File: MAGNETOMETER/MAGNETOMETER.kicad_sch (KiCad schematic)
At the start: 2 parts, among them IC6 MMC5603NJ

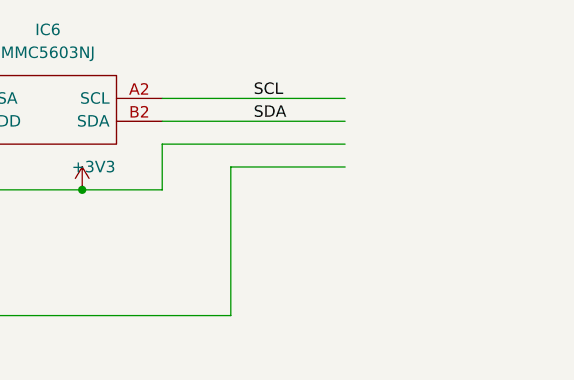
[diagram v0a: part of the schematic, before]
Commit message: Route sensors, IMU and radio board
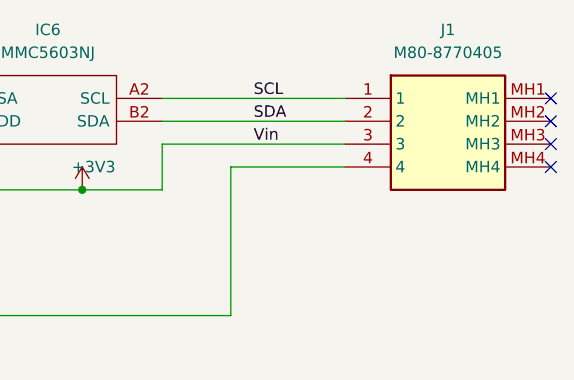
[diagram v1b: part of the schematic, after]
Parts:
- added J1: M80-8770405, M808770405, symbol M80-8770405:M80-8770405
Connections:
- net +3V3: now also J1.3
- net GND: now also J1.4
- net SCL: now also J1.1
- net SDA: now also J1.2
- no-connect marks 0 -> 4
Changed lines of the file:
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@@
   (junction (at 118.11 95.25) (diameter 0) (color 0 0 0 0)
   )
+  (no_connect (at 186.69 87.63))
+  (no_connect (at 186.69 92.71))
+  (no_connect (at 186.69 90.17))
+  (no_connect (at 186.69 85.09))
   (wire (pts (xy 143.51 87.63) (xy 163.83 87.63))
     (stroke (width 0) (type default))
@@
   )
   (label "SCL" (at 153.67 85.09 0) (fields_autoplaced)
+    (effects (font (size 1.27 1.27)) (justify left bottom))
+  )
+  (label "Vin" (at 153.67 90.17 0) (fields_autoplaced)
     (effects (font (size 1.27 1.27)) (justify left bottom))
   )
@@
         )
       )
+    )
+  )
+  (symbol (lib_id "M80-8770405:M80-8770405") (at 163.83 85.09 0) (unit 1)
+    (in_bom yes) (on_board yes) (dnp no) (fields_autoplaced)
+    (property "Reference" "J1" (at 175.26 77.47 0)
+      (effects (font (size 1.27 1.27)))
+    )
+    (property "Value" "M80-8770405" (at 175.26 80.01 0)
+      (effects (font (size 1.27 1.27)))
+    )
+    (property "Footprint" "M808770405" (at 182.88 180.01 0)
+      (effects (font (size 1.27 1.27)) (justify left top) hide)
+    )
+    (property "Datasheet" "https://cdn.harwin.com/pdfs/M80-877.pdf" (at 182.88 280.01 0)
+      (effects (font (size 1.27 1.27)) (justify left top) hide)
+    )
+    (property "Height" "5.56" (at 182.88 480.01 0)
+      (effects (font (size 1.27 1.27)) (justify left top) hide)
+    )
+    (property "Manufacturer_Name" "Harwin" (at 182.88 580.01 0)
+      (effects (font (size 1.27 1.27)) (justify left top) hide)
+    )
+    (property "Manufacturer_Part_Number" "M80-8770405" (at 182.88 680.01 0)
+      (effects (font (size 1.27 1.27)) (justify left top) hide)
+    )
+    (property "Mouser Part Number" "855-M80-8770405" (at 182.88 780.01 0)
+      (effects (font (size 1.27 1.27)) (justify left top) hide)
+    )
+    (property "Mouser Price/Stock" "https://www.mouser.co.uk/ProductDetail/Harwin/M80-8770405?qs=3tymCvhQ29ZPq83M%252Bf8kIA%3D%3D" (at 182.88 880.01 0)
+      (effects (font (size 1.27 1.27)) (justify left top) hide)
+    )
+    (property "Arrow Part Number" "" (at 182.88 980.01 0)
+      (effects (font (size 1.27 1.27)) (justify left top) hide)
+    )
+    (property "Arrow Price/Stock" "" (at 182.88 1080.01 0)
+      (effects (font (size 1.27 1.27)) (justify left top) hide)
+    )
+    (pin "1")
+    (pin "2")
+    (pin "3")
+    (pin "4")
+    (pin "MH1")
+    (pin "MH2")
+    (pin "MH3")
+    (pin "MH4")
+    (instances
+      (project "MAGNETOMETER"
+        (path "/1ff82954-21a9-4f7a-99bd-a8202cea8bb4"
+          (reference "J1") (unit 1)
+        )
+      )

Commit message: Done with most of the boards
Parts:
- added R1, R2: 2.7K, Resistor_SMD:R_0201_0603Metric, symbol Device:R
- J1: footprint M808770405 -> KiCad:M808770405
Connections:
- net SCL: now also R1.2; no longer IC6.A2 (SCL)
- net SDA: now also R2.2; no longer IC6.B2 (SDA)
- new net: IC6.A2 (SCL), R1.1
- new net: IC6.B2 (SDA), R2.1
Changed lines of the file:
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@@
   (no_connect (at 186.69 90.17))
   (no_connect (at 186.69 85.09))
-  (wire (pts (xy 143.51 87.63) (xy 163.83 87.63))
-    (stroke (width 0) (type default))
-  )
   (wire (pts (xy 151.13 109.22) (xy 151.13 92.71))
     (stroke (width 0) (type default))
@@
     (stroke (width 0) (type default))
   )
-  (wire (pts (xy 143.51 85.09) (xy 163.83 85.09))
+  (wire (pts (xy 151.13 87.63) (xy 163.83 87.63))
     (stroke (width 0) (type default))
   )
   (wire (pts (xy 151.13 92.71) (xy 163.83 92.71))
+    (stroke (width 0) (type default))
+  )
+  (wire (pts (xy 151.13 85.09) (xy 163.83 85.09))
     (stroke (width 0) (type default))
   )
@@
         (path "/39d7ebb3-b69d-4ae9-8f55-c9acfe77d345/82e19a29-2001-4834-a54c-a35440bfa66f"
           (reference "C20") (unit 1)
+        )
+      )
+    )
+  )
+  (symbol (lib_id "Device:R") (at 147.32 85.09 90) (unit 1)
+    (in_bom yes) (on_board yes) (dnp no)
+    (property "Reference" "R1" (at 146.05 82.55 0)
+      (effects (font (size 1.27 1.27)) (justify left))
+    )
+    (property "Value" "2.7K" (at 149.86 83.82 0)
+      (effects (font (size 1.27 1.27)) (justify left))
+    )
+    (property "Footprint" "Resistor_SMD:R_0201_0603Metric" (at 147.32 86.868 90)
+      (effects (font (size 1.27 1.27)) hide)
+    )
+    (property "Datasheet" "~" (at 147.32 85.09 0)
+      (effects (font (size 1.27 1.27)) hide)
+    )
+    (pin "1")
+    (pin "2")
+    (instances
+      (project "MAGNETOMETER"
+        (path "/1ff82954-21a9-4f7a-99bd-a8202cea8bb4"
+          (reference "R1") (unit 1)
         )
       )
@@
         (path "/6135eb53-87c0-4516-a6dc-aa2a3e58fdeb"
           (reference "#PWR02") (unit 1)
+        )
+      )
+    )
+  )
+  (symbol (lib_id "Device:R") (at 147.32 87.63 90) (unit 1)
+    (in_bom yes) (on_board yes) (dnp no) (fields_autoplaced)
+    (property "Reference" "R2" (at 147.32 81.28 90)
+      (effects (font (size 1.27 1.27)))
+    )
+    (property "Value" "2.7K" (at 147.32 83.82 90)
+      (effects (font (size 1.27 1.27)))
+    )
+    (property "Footprint" "Resistor_SMD:R_0201_0603Metric" (at 147.32 89.408 90)
+      (effects (font (size 1.27 1.27)) hide)
+    )
+    (property "Datasheet" "~" (at 147.32 87.63 0)
+      (effects (font (size 1.27 1.27)) hide)
+    )
+    (pin "1")
+    (pin "2")
+    (instances
+      (project "MAGNETOMETER"
+        (path "/1ff82954-21a9-4f7a-99bd-a8202cea8bb4"
+          (reference "R2") (unit 1)
         )
       )
@@
       (effects (font (size 1.27 1.27)))
     )
-    (property "Footprint" "M808770405" (at 182.88 180.01 0)
+    (property "Footprint" "KiCad:M808770405" (at 182.88 180.01 0)
       (effects (font (size 1.27 1.27)) (justify left top) hide)
     )

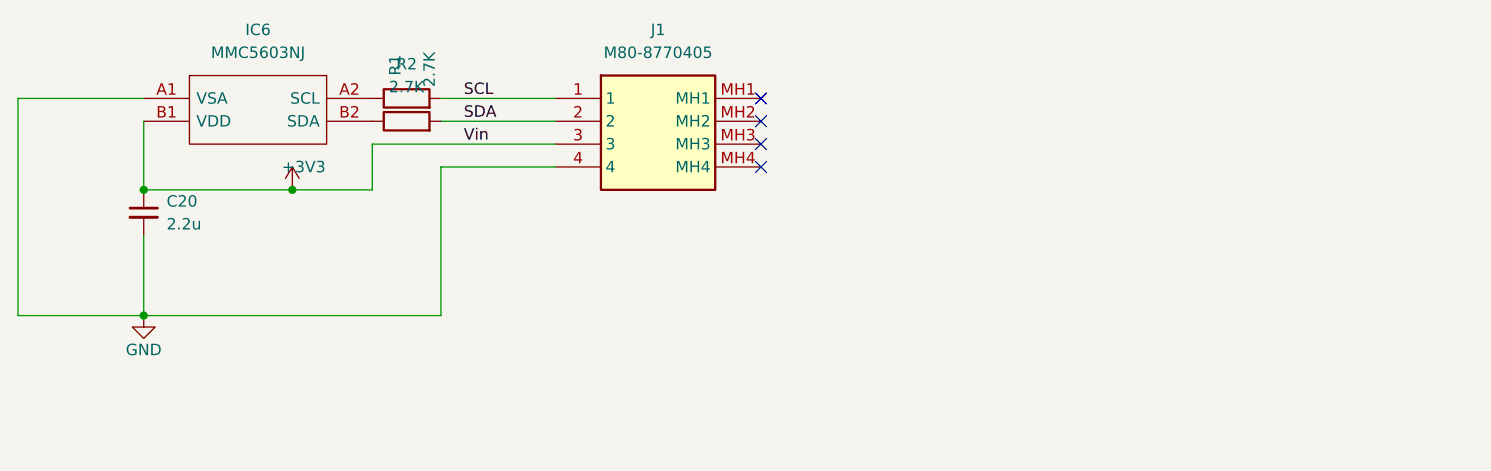
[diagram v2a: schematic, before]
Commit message: Fixed Accel, Barometer, FRAM, Inertia unit, and Magnetometer
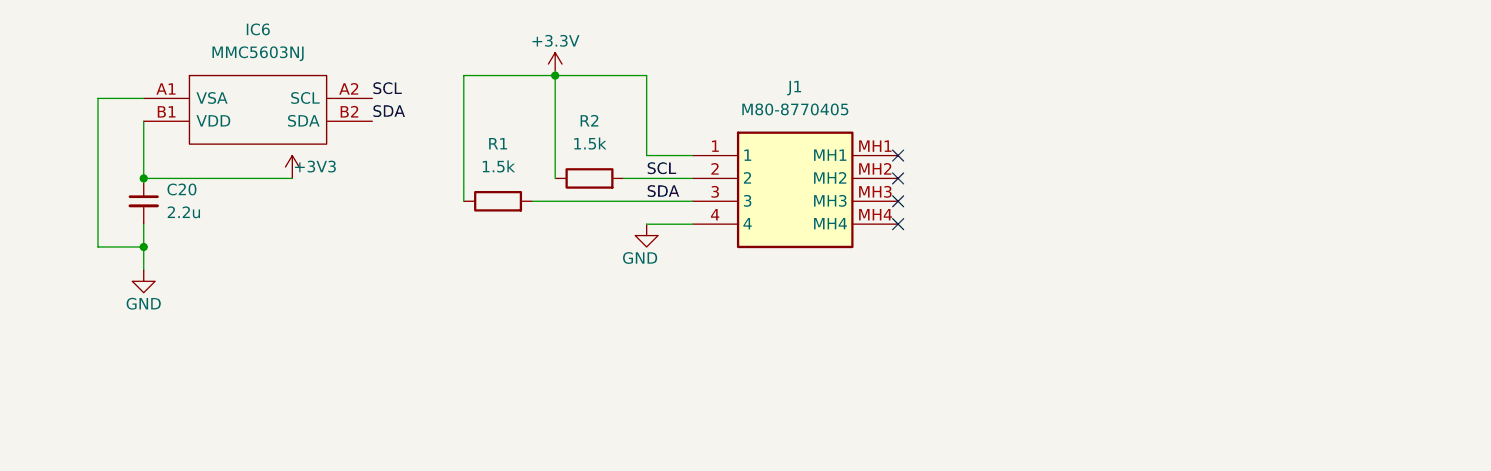
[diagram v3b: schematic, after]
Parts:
- J1: footprint KiCad:M808770405 -> M808770405
- R1, R2: value 2.7K -> 1.5k; footprint Resistor_SMD:R_0201_0603Metric -> Resistor_SMD:R_0201_0603Metric_Pad0.64x0.40mm_HandSolder
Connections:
- net +3V3: no longer J1.3
- net SCL: now also IC6.A2 (SCL), J1.2, R2.2; no longer J1.1, R1.2
- net SDA: now also IC6.B2 (SDA), J1.3, R1.2; no longer J1.2, R2.2
- net +3.3V: now reaches R1.1
- net +3.3V: now also J1.1, R2.1; no longer IC6.A2 (SCL)
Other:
- company: (none) -> USST Avionics
- title: (none) -> Magnetometer
- moved on the sheet: C20

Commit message: LC24 PCBs
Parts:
- removed J1: M80-8770405, M808770405, symbol M80-8770405:M80-8770405
- added H1, H2, H3, H4: MountingHole_Pad, Mounting_Wuerth:Mounting_Wuerth_WA-SMSI-M1.6_H1mm_9774010633, symbol Mechanical:MountingHole_Pad
- added J2: M80-8770422, Harwin-M80-8770422:CONN_M80-87704_HRW, symbol Harwin-M80-8770422:M80-8770422
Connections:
- net +3V3 is gone; now on net +3.3V: C20.1, IC6.B1 (VDD)
- net +3.3V: now also J2.1
- net GND: now also H1.1, H2.1, H3.1, H4.1, J2.4
- net SCL: now also J2.2
- net SDA: now also J2.3
- no-connect marks 4 -> 0
